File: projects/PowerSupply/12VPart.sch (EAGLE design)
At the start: 10 parts, among them IC1 LM2596T, SW1 LSP10

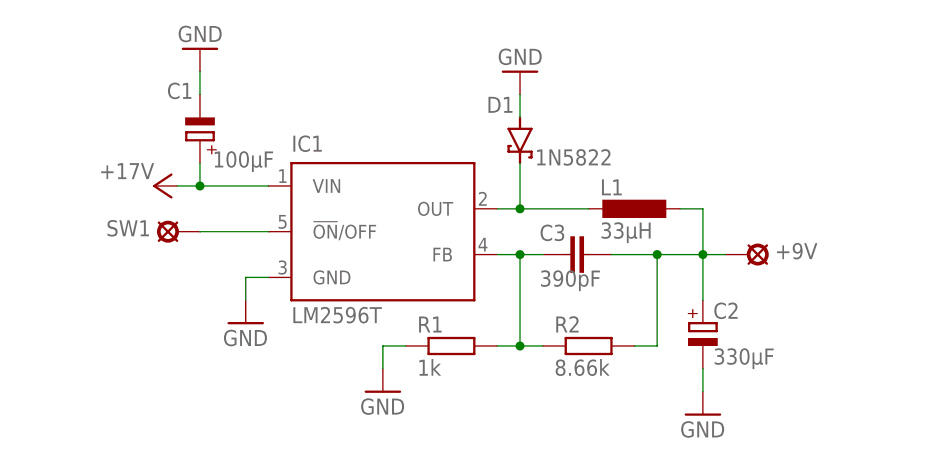
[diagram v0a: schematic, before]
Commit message: feat: power supply
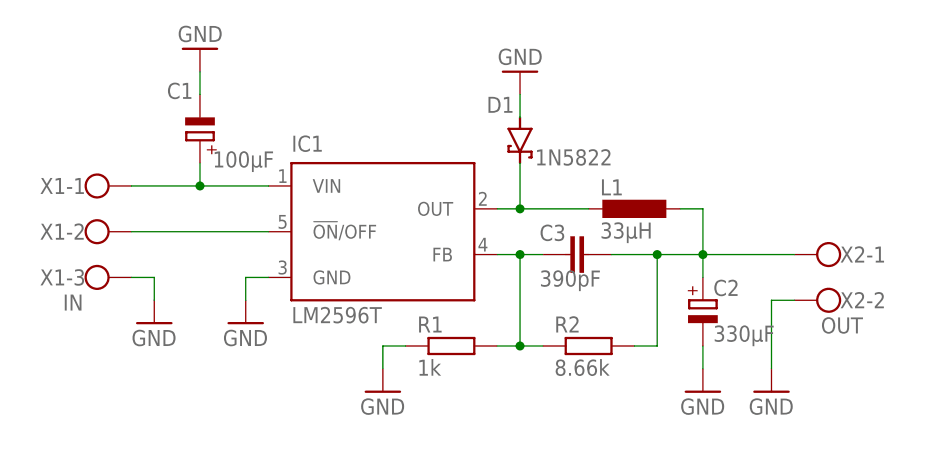
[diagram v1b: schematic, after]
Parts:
- removed +9V, SW1: LSP10, solpad:LSP10
- added X1: IN, con-wago-500:W237-103
- added X2: OUT, con-wago-500:W237-102
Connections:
- removed net VCC: C1.+, IC1.VIN
- new net N$5: C1.+, IC1.VIN, X1-1.KL
- net GND: now also X1-3.KL, X2-2.KL
- net N$2: now also X1-2.KL; no longer SW1.MP
- net N$3: now also X2-1.KL; no longer +9V.MP
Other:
- moved on the sheet: C2

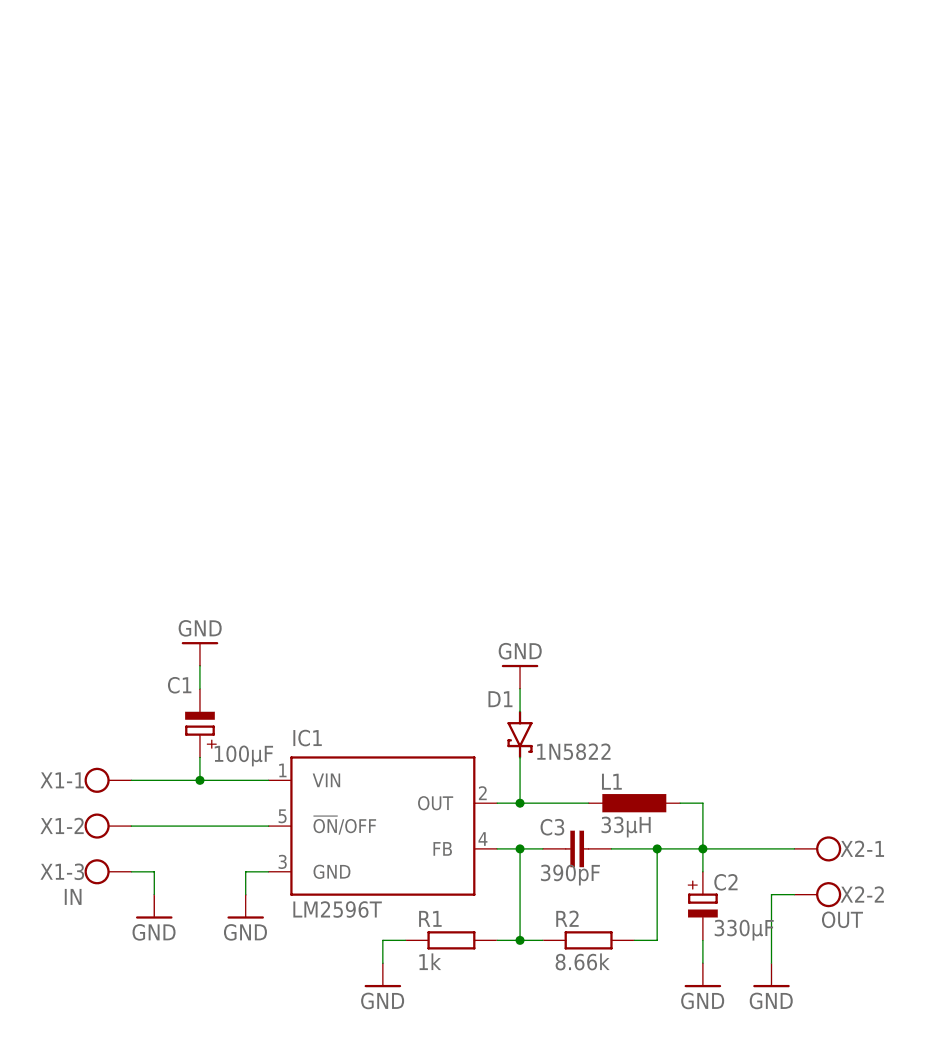
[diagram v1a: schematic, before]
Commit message: feat: power supply
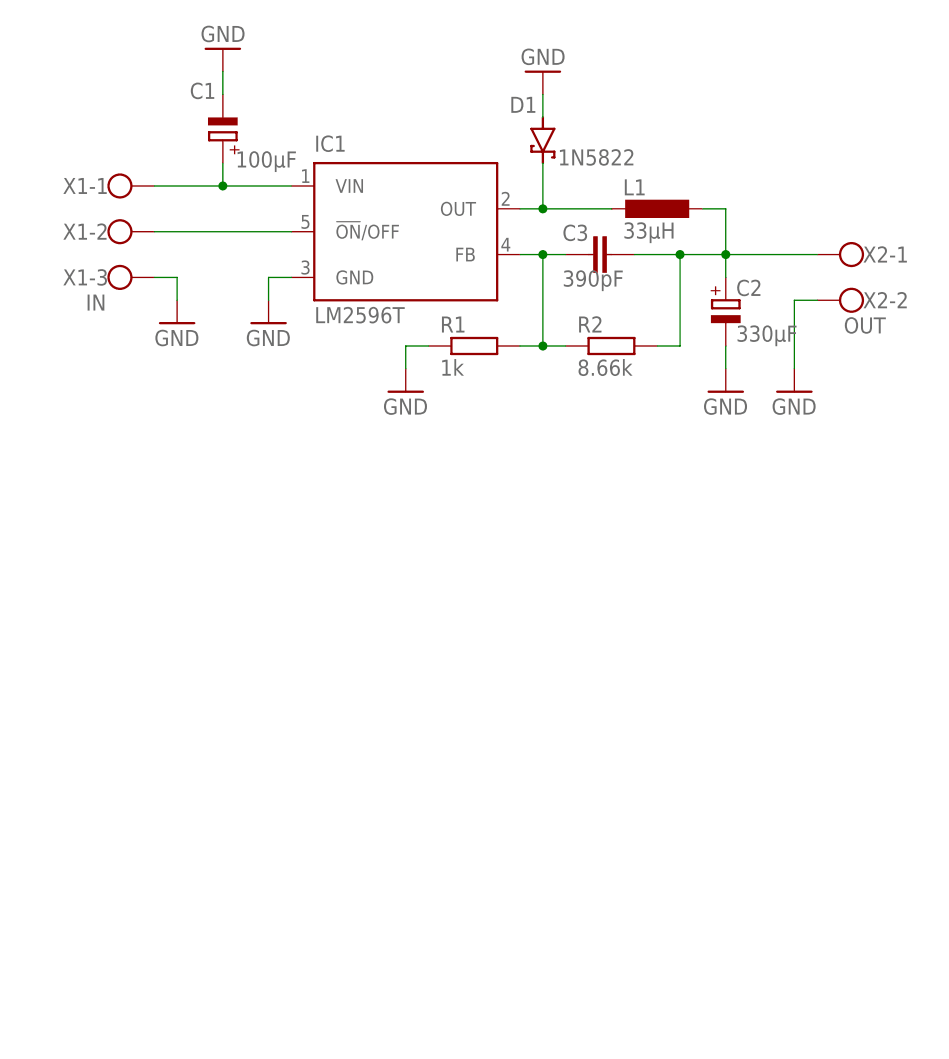
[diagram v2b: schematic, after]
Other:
- moved on the sheet: C1, C2, C3, D1, IC1, L1, R1, R2, X1-1, X1-2, X1-3, X2-1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
